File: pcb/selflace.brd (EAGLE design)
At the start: 25.4 x 47 mm, 45 parts, among them IC1 78L05Z, J3 AVR_SPI_PROG_3X2NS, U1 ATMEGA328P_TQFP, Y1 16MHz

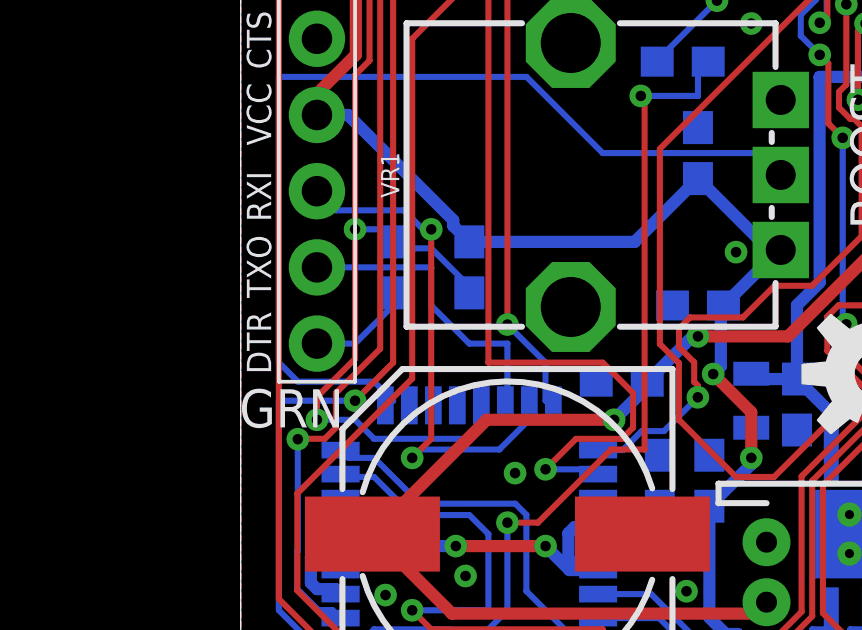
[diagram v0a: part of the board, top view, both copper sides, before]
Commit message: fix rx/tx, not present on in-class pcb
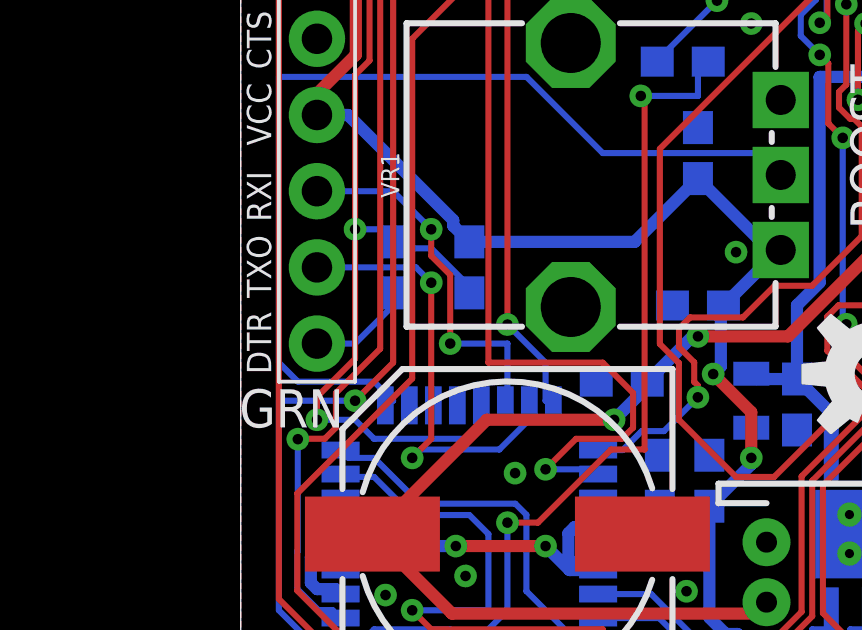
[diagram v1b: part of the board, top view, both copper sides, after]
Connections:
- net RX: now also J4.P$3; no longer J4.P$2
- net TX: now also J4.P$2; no longer J4.P$3
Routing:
- net RX: track 10.2 -> 12.4 mm, vias 0 -> 2
- net TX: track 17.1 -> 15.0 mm
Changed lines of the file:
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@@
 <drawing>
 <settings>
-<setting alwaysvectorfont="yes"/>
+<setting alwaysvectorfont="no"/>
 <setting verticaltext="up"/>
 </settings>
@@
 </signal>
 <signal name="RX">
-<contactref element="J4" pad="P$2"/>
 <contactref element="U1" pad="30"/>
-<wire x1="8.89" y1="17.78" x2="8.89" y2="15.875" width="0.2032" layer="16"/>
-<wire x1="7.62" y1="17.78" x2="8.89" y2="17.78" width="0.2032" layer="16"/>
-<wire x1="6.35" y1="19.05" x2="7.62" y2="17.78" width="0.2032" layer="16"/>
-<wire x1="6.35" y1="20.32" x2="6.35" y2="19.05" width="0.2032" layer="16"/>
-<wire x1="2.54" y1="20.32" x2="6.35" y2="20.32" width="0.2032" layer="16"/>
+<wire x1="8.89" y1="15.875" x2="8.89" y2="17.78" width="0.2032" layer="16"/>
+<wire x1="8.89" y1="17.78" x2="6.9822" y2="17.78" width="0.2032" layer="16"/>
 <wire x1="8.89" y1="15.875" x2="8.82" y2="15.7226" width="0.2032" layer="16"/>
+<contactref element="J4" pad="P$3"/>
+<via x="6.9822" y="17.78" extent="1-16" drill="0.35"/>
+<via x="6.3486" y="21.5886" extent="1-16" drill="0.35"/>
+<wire x1="6.3486" y1="20.70466875" x2="6.3486" y2="21.5886" width="0.2032" layer="1"/>
+<wire x1="6.9822" y1="20.07106875" x2="6.3486" y2="20.70466875" width="0.2032" layer="1"/>
+<wire x1="6.9822" y1="17.78" x2="6.9822" y2="20.07106875" width="0.2032" layer="1"/>
+<wire x1="6.3486" y1="21.5886" x2="5.0772" y2="22.86" width="0.2032" layer="16"/>
+<wire x1="5.0772" y1="22.86" x2="2.54" y2="22.86" width="0.2032" layer="16"/>
 </signal>
 <signal name="TX">
-<contactref element="J4" pad="P$3"/>
 <contactref element="U1" pad="31"/>
 <wire x1="6.35" y1="14.605" x2="5.715" y2="13.97" width="0.2032" layer="1"/>
@@
 <wire x1="8.6204125" y1="14.2494" x2="9.62" y2="15.2489875" width="0.2032" layer="16"/>
 <wire x1="9.62" y1="15.2489875" x2="9.62" y2="15.7226" width="0.2032" layer="16"/>
-<via x="6.35" y="21.5872" extent="1-16" drill="0.35"/>
-<wire x1="2.54" y1="22.86" x2="3.1778" y2="22.2222" width="0.2032" layer="16"/>
-<wire x1="6.0720125" y1="21.5872" x2="6.35" y2="21.5872" width="0.2032" layer="16"/>
-<wire x1="3.1778" y1="22.2222" x2="5.4370125" y2="22.2222" width="0.2032" layer="16"/>
-<wire x1="5.4370125" y1="22.2222" x2="6.0720125" y2="21.5872" width="0.2032" layer="16"/>
-<wire x1="6.35" y1="21.5872" x2="6.35" y2="14.605" width="0.2032" layer="1"/>
+<via x="6.35" y="19.8092" extent="1-16" drill="0.35"/>
+<wire x1="6.35" y1="19.8092" x2="6.35" y2="14.605" width="0.2032" layer="1"/>
+<contactref element="J4" pad="P$2"/>
+<wire x1="2.54" y1="20.32" x2="5.8392" y2="20.32" width="0.2032" layer="16"/>
+<wire x1="5.8392" y1="20.32" x2="6.35" y2="19.8092" width="0.2032" layer="16"/>
 </signal>
 <signal name="DTR">
